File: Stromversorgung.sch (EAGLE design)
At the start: 17 parts, among them IC1 LM2574N-3.3, X1 MSTBV4, X2 Power ext., 5V 1A, X4 Power int., 5V 3A

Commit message: Pi und Stromversorgung Rev. 2019
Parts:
- removed C1: 22µF 75V, rcl:CPOL-EUE2.5-5
- removed C2: 220µF 25V, rcl:CPOL-EUE2.5-5
- removed D1: 1N5819-B, diode:1N5819-B
- removed IC1: LM2574N-3.3, linear:LM2574N-3.3
- removed L1: 100µH, rcl:L-EU6000-XXX-RC
- removed SV1: PLATINENVERBINDER-31SMD, homepi:PLATINENVERBINDER-31SMD
- removed X4: Power int., 5V 3A, con-phoenix-508:MSTBV2
- added J1: DCJ0202, con-jack:DCJ0202
- added U1, U3: TSR_2-2450, _traco_tsr-1:TSR_1-2450
- added U2: TSR_0.5-2433, _traco_tsr-1:TSR_1-2433
- X1: value MSTBV4 -> Ein/Aus; device con-phoenix-508:MSTBV4 -> con-phoenix-508:MSTBV2
- X2: value Power ext., 5V 1A -> MAC64L; device con-phoenix-508:MSTBV2 -> con-vg:MAC64L
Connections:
- removed net +3,3V_INT_1: C2.+, IC1.FB, JP2.2, L1.1
- removed net GND_EXT: LED3.C, SV1.30, X2-1.1
- removed net GND_INT: C1.-, C2.-, D1.A, IC1.!ON/OFF, IC1.GND@PWR, IC1.GNDSIG, LED1.C, LED2.C, SV1.29, SV1.3, SV1.6, SV1.8, X4-1.1
- removed net LM2574_IN: C1.+, IC1.IN, JP1.1
- removed net LM2574_OUT: D1.C, IC1.OUT, L1.2
- removed net N$3: X1-3.1, X4-2.1
- new net +24V: JP1.2, U1.VI, U3.VI, X1-1.1, X2.A32, X2.C32
- new net GND: J1.3, LED1.C, LED2.C, LED3.C, U1.GND, U2.GND, U3.GND, X2.A29, X2.A3, X2.A30, X2.A6, X2.A8, X2.C29, X2.C3, X2.C30, X2.C6, X2.C8
- new net N$2: JP2.2, U2.VO
- new net VI: JP1.1, U2.VI
- net +3,3V: now also X2.A2, X2.C2; no longer SV1.2
- net +5V_EXT: now also U3.VO, X2.A31, X2.C31; no longer SV1.31, X1-2.1
- net +5V_INT: now also U1.VO, X2.A1, X2.A28, X2.C1, X2.C28; no longer JP1.2, SV1.1, SV1.28, X1-4.1
- net N$1: now also J1.1, X1-2.1; no longer X1-1.1, X2-2.1
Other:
- moved on the sheet: JP1, JP2, LED1, LED2, LED3, R1, R2, R3, X1-1, X1-2

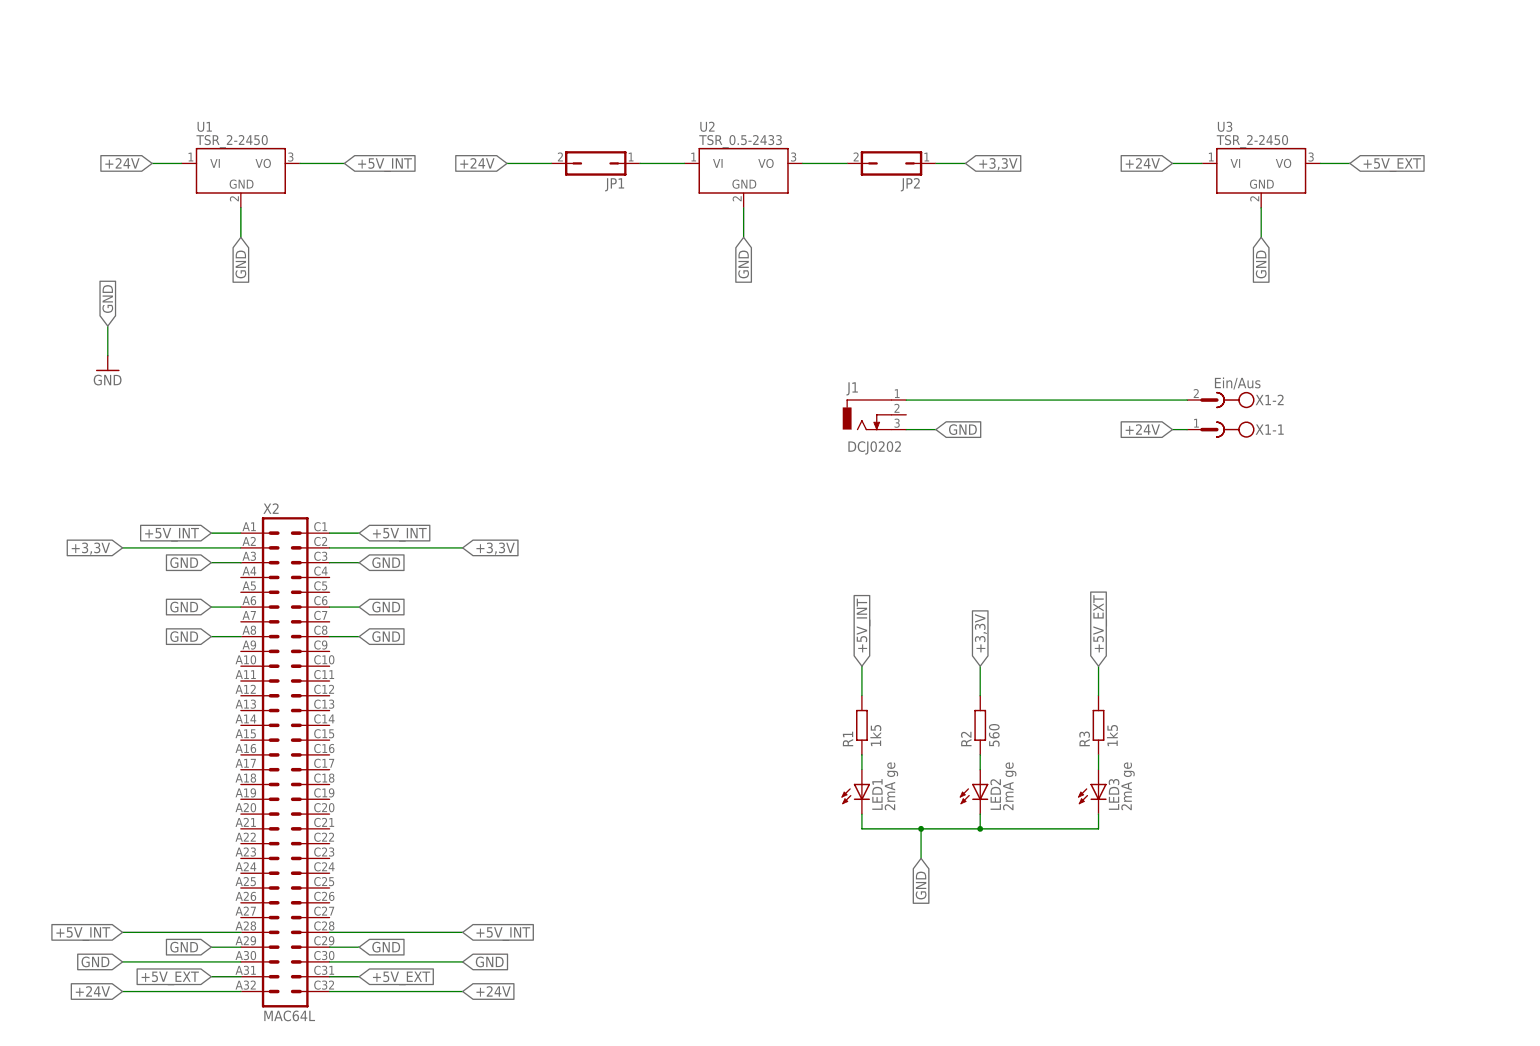
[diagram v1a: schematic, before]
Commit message: Anpassungen an Rev. 2019, erste Can-Bus Elemente
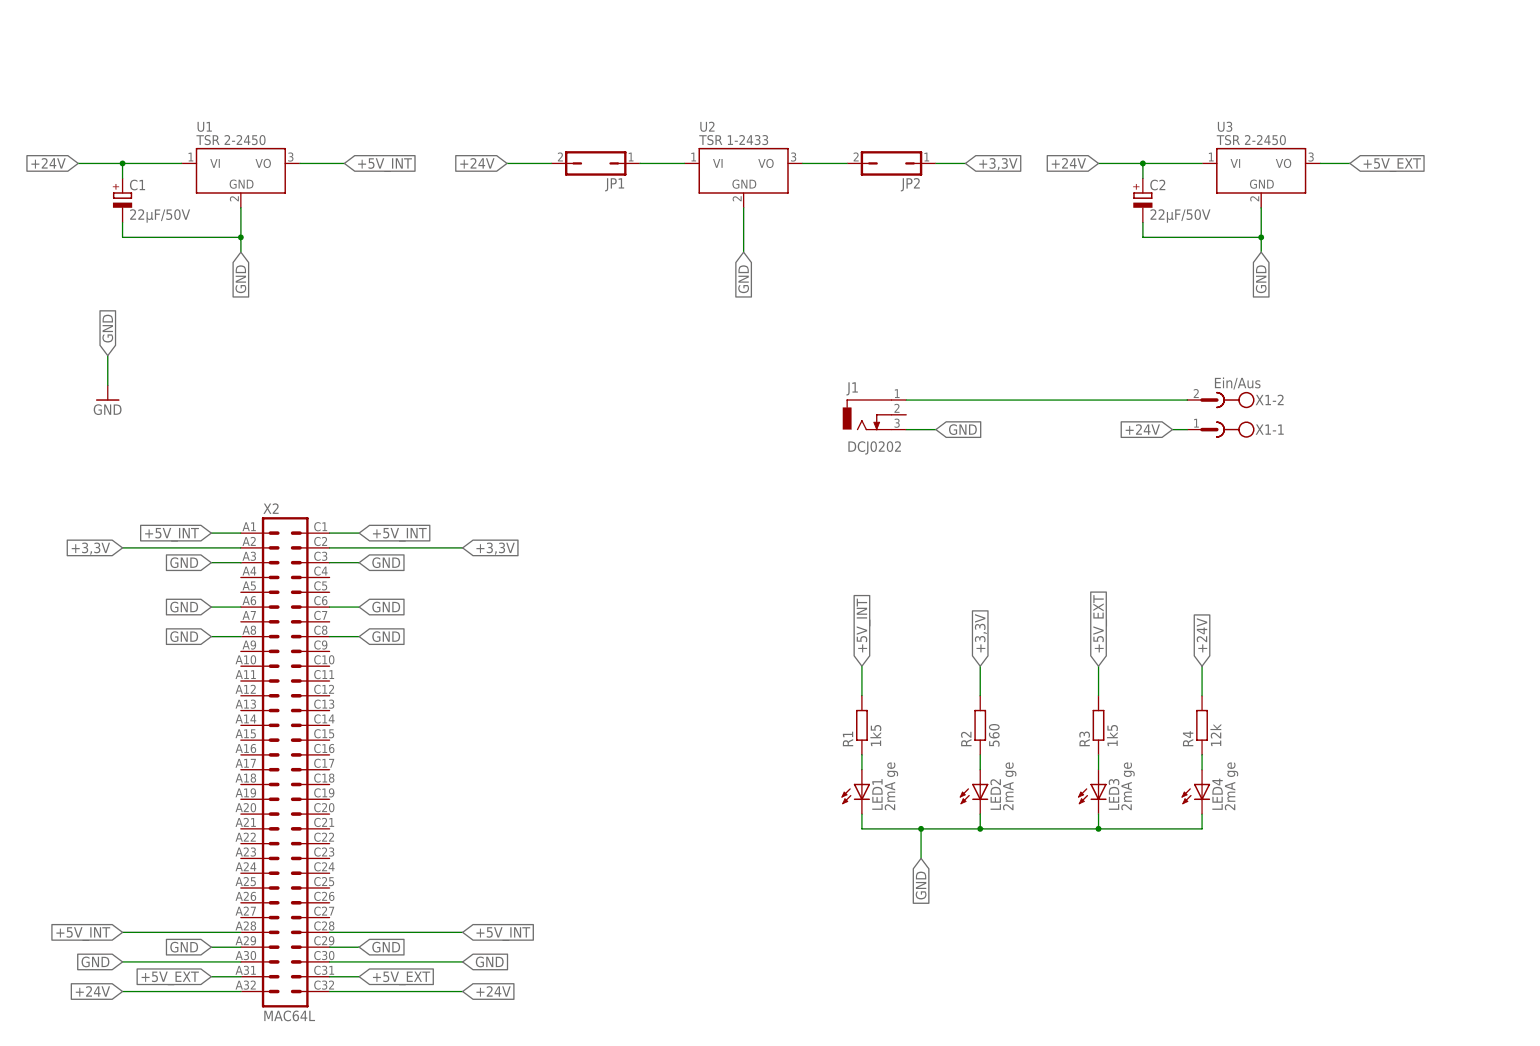
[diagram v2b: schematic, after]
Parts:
- added C1, C2: 22µF/50V, rcl:CPOL-EUE2-5
- added LED4: 2mA ge, led:LED3MM
- added R4: 12k, rcl:R-EU_0204/5
- U1, U3: value TSR_2-2450 -> TSR 2-2450
- U2: value TSR_0.5-2433 -> TSR 1-2433
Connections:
- new net N$3: LED4.A, R4.1
- net +24V: now also C1.+, C2.+, R4.2
- net GND: now also C1.-, C2.-, LED4.C
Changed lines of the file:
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@@
 <part name="R2" library="rcl" deviceset="R-EU_" device="0204/5" value="560"/>
 <part name="R3" library="rcl" deviceset="R-EU_" device="0204/5" value="1k5"/>
-<part name="U1" library="_traco_tsr-1" deviceset="TSR_1-*" device="" technology="2450" value="TSR_2-2450"/>
-<part name="U2" library="_traco_tsr-1" deviceset="TSR_1-*" device="" technology="2433" value="TSR_0.5-2433"/>
-<part name="U3" library="_traco_tsr-1" deviceset="TSR_1-*" device="" technology="2450" value="TSR_2-2450"/>
+<part name="U1" library="_traco_tsr-1" deviceset="TSR_1-*" device="" technology="2450" value="TSR 2-2450"/>
+<part name="U2" library="_traco_tsr-1" deviceset="TSR_1-*" device="" technology="2433" value="TSR 1-2433"/>
+<part name="U3" library="_traco_tsr-1" deviceset="TSR_1-*" device="" technology="2450" value="TSR 2-2450"/>
 <part name="FRAME1" library="frames" deviceset="A4L-LOC" device=""/>
 <part name="GND1" library="supply1" deviceset="GND" device=""/>
 <part name="J1" library="con-jack" deviceset="DCJ0202" device=""/>
 <part name="X2" library="con-vg" deviceset="MAC64L" device=""/>
+<part name="C1" library="rcl" deviceset="CPOL-EU" device="E2-5" value="22µF/50V"/>
+<part name="C2" library="rcl" deviceset="CPOL-EU" device="E2-5" value="22µF/50V"/>
+<part name="R4" library="rcl" deviceset="R-EU_" device="0204/5" value="12k"/>
+<part name="LED4" library="led" deviceset="LED" device="3MM" value="2mA ge"/>
 </parts>
 <sheets>
@@
 <instance part="U3" gate="G$1" x="213.36" y="152.4"/>
 <instance part="FRAME1" gate="G$1" x="-5.08" y="-5.08"/>
-<instance part="GND1" gate="1" x="15.24" y="116.84"/>
+<instance part="GND1" gate="1" x="15.24" y="111.76"/>
 <instance part="J1" gate="G$1" x="144.78" y="109.22"/>
 <instance part="X2" gate="G$1" x="45.72" y="50.8"/>
+<instance part="C1" gate="G$1" x="17.78" y="147.32"/>
+<instance part="C2" gate="G$1" x="193.04" y="147.32"/>
+<instance part="R4" gate="G$1" x="203.2" y="55.88" rot="R90"/>
+<instance part="LED4" gate="G$1" x="203.2" y="45.72"/>
 </instances>
 <busses>
@@
 <segment>
 <pinref part="U1" gate="G$1" pin="VI"/>
-<wire x1="27.94" y1="152.4" x2="22.86" y2="152.4" width="0.1524" layer="91"/>
-<label x="22.86" y="152.4" size="1.778" layer="95" rot="R180" xref="yes"/>
+<wire x1="27.94" y1="152.4" x2="17.78" y2="152.4" width="0.1524" layer="91"/>
+<label x="10.16" y="152.4" size="1.778" layer="95" rot="R180" xref="yes"/>
+<pinref part="C1" gate="G$1" pin="+"/>
+<wire x1="17.78" y1="152.4" x2="10.16" y2="152.4" width="0.1524" layer="91"/>
+<wire x1="17.78" y1="149.86" x2="17.78" y2="152.4" width="0.1524" layer="91"/>
+<junction x="17.78" y="152.4"/>
 </segment>
 <segment>
 <pinref part="U3" gate="G$1" pin="VI"/>
-<wire x1="203.2" y1="152.4" x2="198.12" y2="152.4" width="0.1524" layer="91"/>
-<label x="198.12" y="152.4" size="1.778" layer="95" rot="R180" xref="yes"/>
+<wire x1="203.2" y1="152.4" x2="193.04" y2="152.4" width="0.1524" layer="91"/>
+<label x="185.42" y="152.4" size="1.778" layer="95" rot="R180" xref="yes"/>
+<pinref part="C2" gate="G$1" pin="+"/>
+<wire x1="193.04" y1="152.4" x2="185.42" y2="152.4" width="0.1524" layer="91"/>
+<wire x1="193.04" y1="149.86" x2="193.04" y2="152.4" width="0.1524" layer="91"/>
+<junction x="193.04" y="152.4"/>
 </segment>
 <segment>
@@
 <label x="198.12" y="106.68" size="1.778" layer="95" rot="R180" xref="yes"/>
 </segment>
+<segment>
+<pinref part="R4" gate="G$1" pin="2"/>
+<wire x1="203.2" y1="60.96" x2="203.2" y2="66.04" width="0.1524" layer="91"/>
+<label x="203.2" y="66.04" size="1.778" layer="95" rot="R90" xref="yes"/>
+</segment>
 </net>
 <net name="GND" class="0">
 <segment>
 <pinref part="GND1" gate="1" pin="GND"/>
-<wire x1="15.24" y1="119.38" x2="15.24" y2="124.46" width="0.1524" layer="91"/>
-<label x="15.24" y="124.46" size="1.778" layer="95" rot="R90" xref="yes"/>
+<wire x1="15.24" y1="114.3" x2="15.24" y2="119.38" width="0.1524" layer="91"/>
+<label x="15.24" y="119.38" size="1.778" layer="95" rot="R90" xref="yes"/>
 </segment>
 <segment>
 <pinref part="U1" gate="G$1" pin="GND"/>
 <wire x1="38.1" y1="144.78" x2="38.1" y2="139.7" width="0.1524" layer="91"/>
-<label x="38.1" y="139.7" size="1.778" layer="95" rot="R270" xref="yes"/>
+<label x="38.1" y="137.16" size="1.778" layer="95" rot="R270" xref="yes"/>
+<pinref part="C1" gate="G$1" pin="-"/>
+<wire x1="38.1" y1="139.7" x2="38.1" y2="137.16" width="0.1524" layer="91"/>
+<wire x1="17.78" y1="142.24" x2="17.78" y2="139.7" width="0.1524" layer="91"/>
+<wire x1="17.78" y1="139.7" x2="38.1" y2="139.7" width="0.1524" layer="91"/>
+<junction x="38.1" y="139.7"/>
 </segment>
 <segment>
 <pinref part="U2" gate="G$1" pin="GND"/>
-<wire x1="124.46" y1="144.78" x2="124.46" y2="139.7" width="0.1524" layer="91"/>
-<label x="124.46" y="139.7" size="1.778" layer="95" rot="R270" xref="yes"/>
+<wire x1="124.46" y1="144.78" x2="124.46" y2="137.16" width="0.1524" layer="91"/>
+<label x="124.46" y="137.16" size="1.778" layer="95" rot="R270" xref="yes"/>
 </segment>
 <segment>
 <pinref part="U3" gate="G$1" pin="GND"/>
 <wire x1="213.36" y1="144.78" x2="213.36" y2="139.7" width="0.1524" layer="91"/>
-<label x="213.36" y="139.7" size="1.778" layer="95" rot="R270" xref="yes"/>
+<label x="213.36" y="137.16" size="1.778" layer="95" rot="R270" xref="yes"/>
+<pinref part="C2" gate="G$1" pin="-"/>
+<wire x1="213.36" y1="139.7" x2="213.36" y2="137.16" width="0.1524" layer="91"/>
+<wire x1="193.04" y1="142.24" x2="193.04" y2="139.7" width="0.1524" layer="91"/>
+<wire x1="193.04" y1="139.7" x2="213.36" y2="139.7" width="0.1524" layer="91"/>
+<junction x="213.36" y="139.7"/>
 </segment>
 <segment>
@@
 <wire x1="185.42" y1="38.1" x2="165.1" y2="38.1" width="0.1524" layer="91"/>
 <junction x="165.1" y="38.1"/>
+<pinref part="LED4" gate="G$1" pin="C"/>
+<wire x1="185.42" y1="38.1" x2="203.2" y2="38.1" width="0.1524" layer="91"/>
+<wire x1="203.2" y1="38.1" x2="203.2" y2="40.64" width="0.1524" layer="91"/>
+<junction x="185.42" y="38.1"/>
 </segment>
 <segment>
@@
 </segment>
 </net>
+<net name="N$3" class="0">
+<segment>
+<pinref part="LED4" gate="G$1" pin="A"/>
+<pinref part="R4" gate="G$1" pin="1"/>
+<wire x1="203.2" y1="48.26" x2="203.2" y2="50.8" width="0.1524" layer="91"/>
+</segment>
+</net>

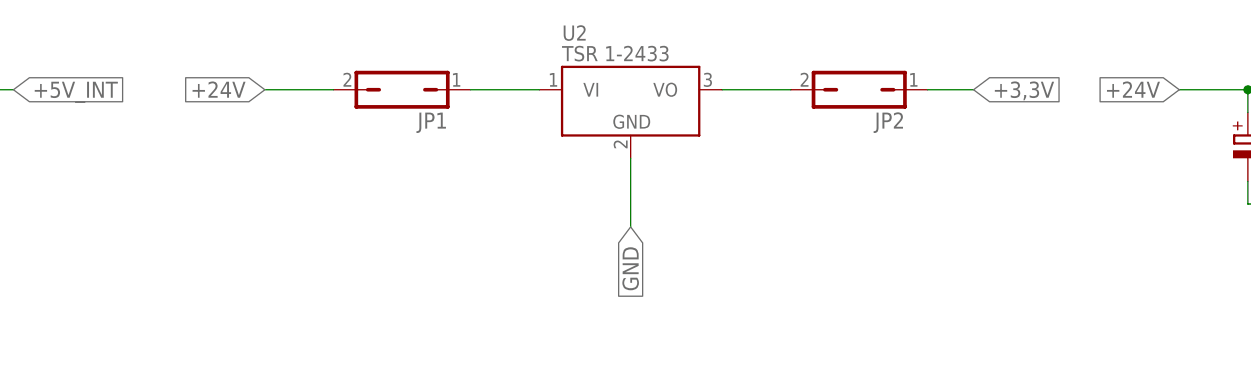
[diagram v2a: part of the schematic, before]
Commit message: 3,3V-Versorgung nur noch über TSR-Spannungsregler
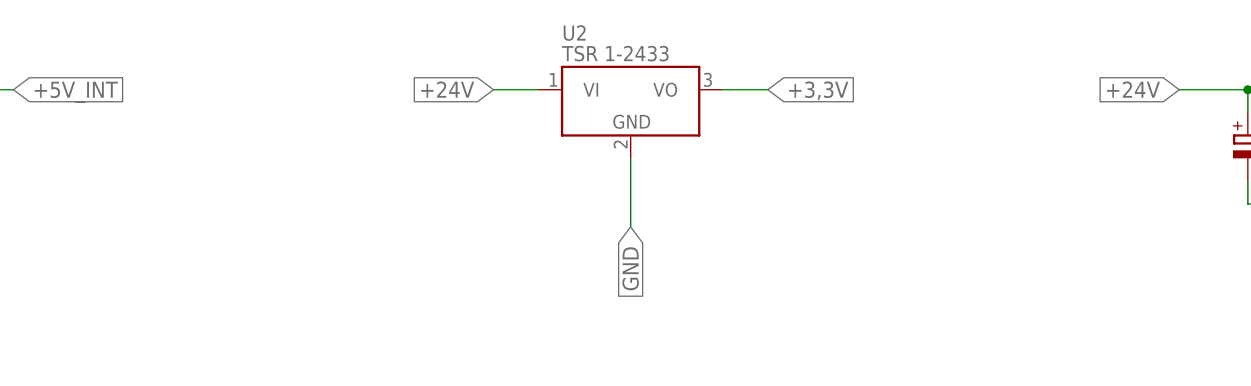
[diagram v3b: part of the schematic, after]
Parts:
- removed JP1, JP2: (no value), jumper:JP1Q
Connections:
- removed net N$2: JP2.2, U2.VO
- removed net VI: JP1.1, U2.VI
- net +24V: now also U2.VI; no longer JP1.2
- net +3,3V: now also U2.VO; no longer JP2.1
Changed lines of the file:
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@@
 <parts>
 <part name="X1" library="con-phoenix-508" deviceset="MSTBV2" device="" value="Ein/Aus"/>
-<part name="JP1" library="jumper" deviceset="JP1Q" device=""/>
-<part name="JP2" library="jumper" deviceset="JP1Q" device=""/>
 <part name="LED1" library="led" deviceset="LED" device="3MM" value="2mA ge"/>
 <part name="LED2" library="led" deviceset="LED" device="3MM" value="2mA ge"/>
@@
 <instance part="R2" gate="G$1" x="165.1" y="55.88" rot="R90"/>
 <instance part="R3" gate="G$1" x="185.42" y="55.88" rot="R90"/>
-<instance part="JP1" gate="A" x="99.06" y="152.4" rot="R90"/>
-<instance part="JP2" gate="A" x="149.86" y="152.4" rot="R90"/>
 <instance part="U1" gate="G$1" x="38.1" y="152.4"/>
 <instance part="U2" gate="G$1" x="124.46" y="152.4"/>
@@
 </segment>
 <segment>
-<pinref part="JP2" gate="A" pin="1"/>
-<wire x1="157.48" y1="152.4" x2="162.56" y2="152.4" width="0.1524" layer="91"/>
-<label x="162.56" y="152.4" size="1.778" layer="95" xref="yes"/>
+<label x="139.7" y="152.4" size="1.778" layer="95" xref="yes"/>
+<pinref part="U2" gate="G$1" pin="VO"/>
+<wire x1="134.62" y1="152.4" x2="139.7" y2="152.4" width="0.1524" layer="91"/>
 </segment>
 <segment>
@@
 </segment>
 </net>
-<net name="N$2" class="0">
-<segment>
-<pinref part="U2" gate="G$1" pin="VO"/>
-<pinref part="JP2" gate="A" pin="2"/>
-<wire x1="134.62" y1="152.4" x2="142.24" y2="152.4" width="0.1524" layer="91"/>
-</segment>
-</net>
-<net name="VI" class="0">
-<segment>
-<pinref part="JP1" gate="A" pin="1"/>
-<pinref part="U2" gate="G$1" pin="VI"/>
-<wire x1="106.68" y1="152.4" x2="114.3" y2="152.4" width="0.1524" layer="91"/>
-</segment>
-</net>
 <net name="+24V" class="0">
-<segment>
-<pinref part="JP1" gate="A" pin="2"/>
-<wire x1="91.44" y1="152.4" x2="83.82" y2="152.4" width="0.1524" layer="91"/>
-<label x="83.82" y="152.4" size="1.778" layer="95" rot="R180" xref="yes"/>
-</segment>
 <segment>
 <pinref part="U1" gate="G$1" pin="VI"/>
@@
 <label x="203.2" y="66.04" size="1.778" layer="95" rot="R90" xref="yes"/>
 </segment>
+<segment>
+<pinref part="U2" gate="G$1" pin="VI"/>
+<wire x1="109.22" y1="152.4" x2="114.3" y2="152.4" width="0.1524" layer="91"/>
+<label x="109.22" y="152.4" size="1.778" layer="95" rot="R180" xref="yes"/>
+</segment>
 </net>
